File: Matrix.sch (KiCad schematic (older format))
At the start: 115 parts

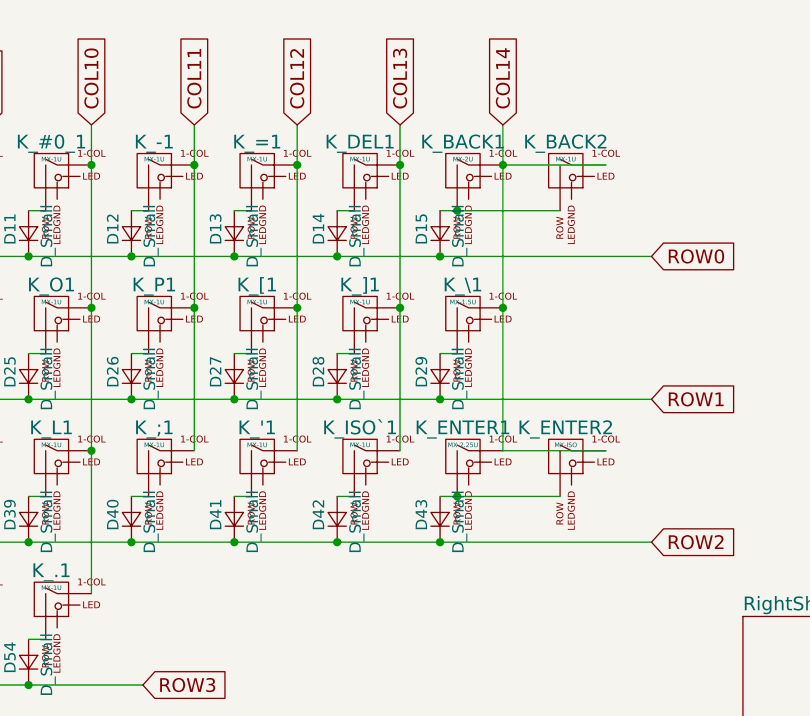
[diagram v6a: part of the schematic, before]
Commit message: Join '\' key and ISO '~' key together to save diode
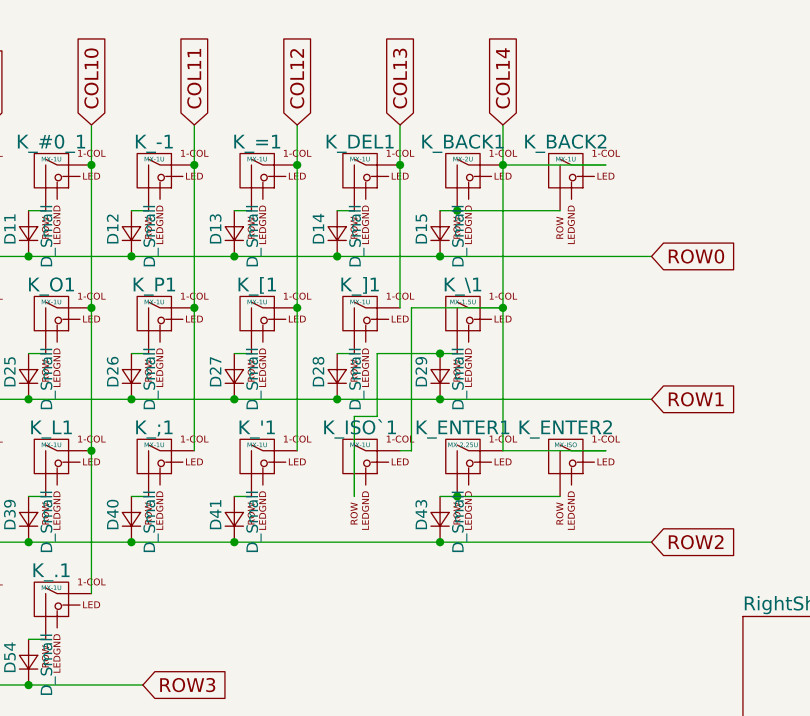
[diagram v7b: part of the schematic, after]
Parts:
- removed D42: D_Small, Diodes_SMD:D_SOD-123, symbol D_Small
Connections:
- net COL13: no longer K_ISO`1.1 (COL)
- net COL14: now also K_ISO`1.1 (COL)
- net at D29.2 (A), K_\1.2 (ROW): now also K_ISO`1.2 (ROW)
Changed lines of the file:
@@
-$EndComp
-$Comp
-L D_Small D42
-U 1 1 5A64987B
-P 7250 2750
-F 0 "D42" H 7200 2830 50  0000 L CNN
-F 1 "D_Small" H 7100 2670 50  0000 L CNN
-F 2 "Diodes_SMD:D_SOD-123" V 7250 2750 50  0001 C CNN
-F 3 "" V 7250 2750 50  0001 C CNN
-	1    7250 2750
-	0    -1   -1   0
 $EndComp
 $Comp
@@
 	7325 2025 7250 2025
 Wire Wire Line
-	7775 2025 7700 2025
+	7425 2025 7775 2025
 Wire Wire Line
 	1225 2650 1475 2650
@@
 Wire Wire Line
 	6875 2650 6800 2650
-Wire Wire Line
-	7325 2650 7250 2650
 Wire Wire Line
 	7700 2650 8225 2650
@@
 Connection ~ 7075 1200
 Wire Wire Line
-	7525 1025 7525 2450
+	7525 1025 7525 1825
 Connection ~ 7525 1200
-Connection ~ 7525 1825
 Wire Wire Line
 	7975 1025 7975 2450
@@
 Connection ~ 6350 2850
 Connection ~ 6800 2850
-Connection ~ 7250 2850
 Wire Wire Line
 	1400 3475 6400 3475
@@
 Connection ~ 3775 3225
 Connection ~ 4225 3225
+Wire Wire Line
+	7425 2025 7425 2300
+Wire Wire Line
+	7425 2300 7325 2300
+Wire Wire Line
+	7325 2300 7325 2650
+Connection ~ 7700 2025
+Wire Wire Line
+	7975 1825 7575 1825
+Wire Wire Line
+	7575 1825 7575 2450
+Wire Wire Line
+	7575 2450 7525 2450
 $EndSCHEMATC
